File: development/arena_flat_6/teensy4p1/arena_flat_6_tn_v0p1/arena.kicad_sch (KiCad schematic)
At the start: 30 parts, among them J1 Barrel_Jack, J2 Conn_01x04_Pin, J3 Conn_01x04_Pin, P1 CONN15, P2 CONN15, P3 CONN15, P4 CONN15, P5 CONN15, P6 CONN15, Q2 MOSFET_NCHAN, SW1 SW_SPDT, U1 SPARKFUN_TXB0104, U2 SPARKFUN_TXB0104, U3 SPARKFUN_TXB0104, U4 SPARKFUN_TXB0104, U5 SPARKFUN_TXB0104, U6 SPARKFUN_TXB0104, U7 Teensy4.1

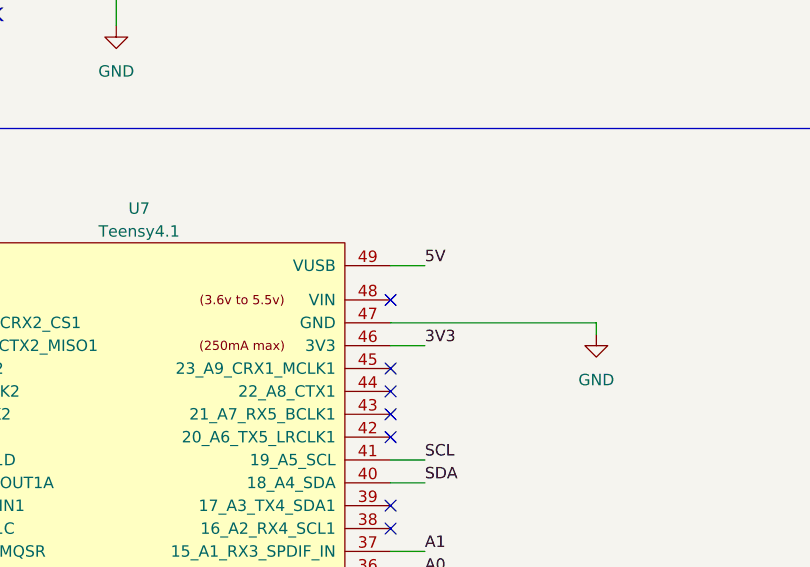
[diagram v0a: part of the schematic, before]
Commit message: Fixed issue on teensy flat 6 arena + more project reorganization.
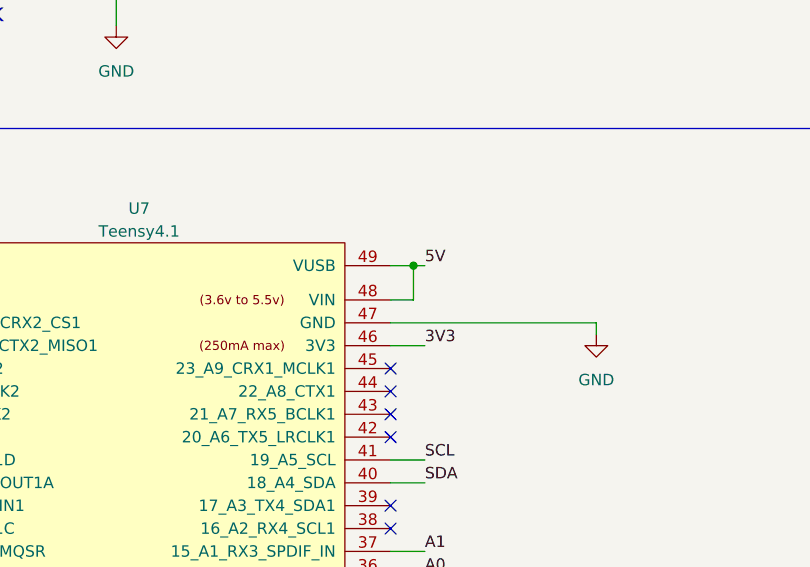
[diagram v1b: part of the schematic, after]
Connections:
- net 5V: now also U7.48 (VIN)
- no-connect marks 71 -> 70
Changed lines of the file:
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@@
   (junction (at 166.37 175.26) (diameter 0) (color 0 0 0 0)
+  )
+  (junction (at 114.3 214.63) (diameter 0) (color 0 0 0 0)
   )
   (junction (at 81.28 182.88) (diameter 0) (color 0 0 0 0)
@@
   (no_connect (at 55.88 220.98))
   (no_connect (at 55.88 284.48))
-  (no_connect (at 111.76 218.44))
   (no_connect (at 111.76 285.75))
   (no_connect (at 254 113.03))
@@
     (stroke (width 0) (type default))
   )
+  (wire (pts (xy 114.3 214.63) (xy 115.57 214.63))
+    (stroke (width 0) (type default))
+  )
   (wire (pts (xy 52.07 251.46) (xy 55.88 251.46))
     (stroke (width 0) (type default))
@@
     (stroke (width 0) (type default))
   )
+  (wire (pts (xy 114.3 218.44) (xy 114.3 214.63))
+    (stroke (width 0) (type default))
+  )
   (wire (pts (xy 132.08 95.25) (xy 132.08 91.44))
     (stroke (width 0) (type default))
@@
     (stroke (width 0) (type default))
   )
+  (wire (pts (xy 111.76 218.44) (xy 114.3 218.44))
+    (stroke (width 0) (type default))
+  )
   (wire (pts (xy 184.15 91.44) (xy 187.96 91.44))
     (stroke (width 0) (type default))
@@
     (stroke (width 0) (type default))
   )
-  (wire (pts (xy 111.76 214.63) (xy 115.57 214.63))
-    (stroke (width 0) (type default))
-  )
+  (wire (pts (xy 111.76 214.63) (xy 114.3 214.63))
+    (stroke (width 0) (type default))
+  )
